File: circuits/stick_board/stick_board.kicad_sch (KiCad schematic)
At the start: 8 parts, among them U1 GULI, U2 GULI, U5 DRV5055A1xDBZxQ1, U6 DRV5055A1xDBZxQ1

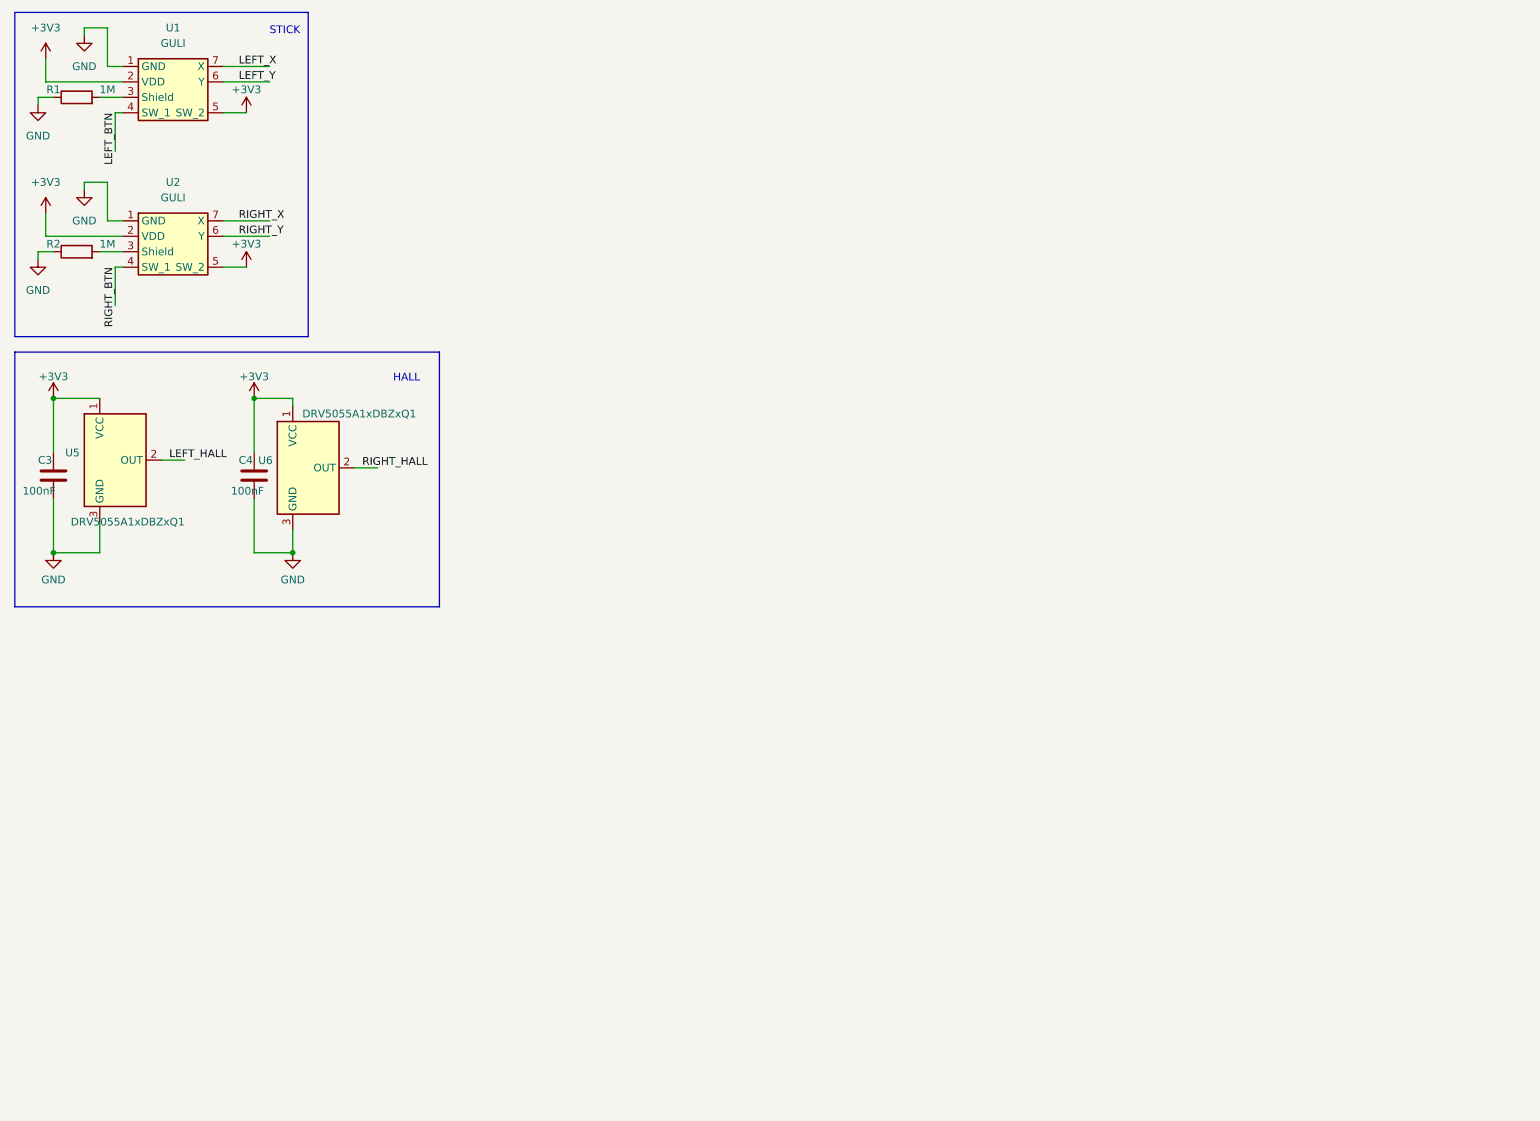
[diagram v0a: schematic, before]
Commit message: add mcu board
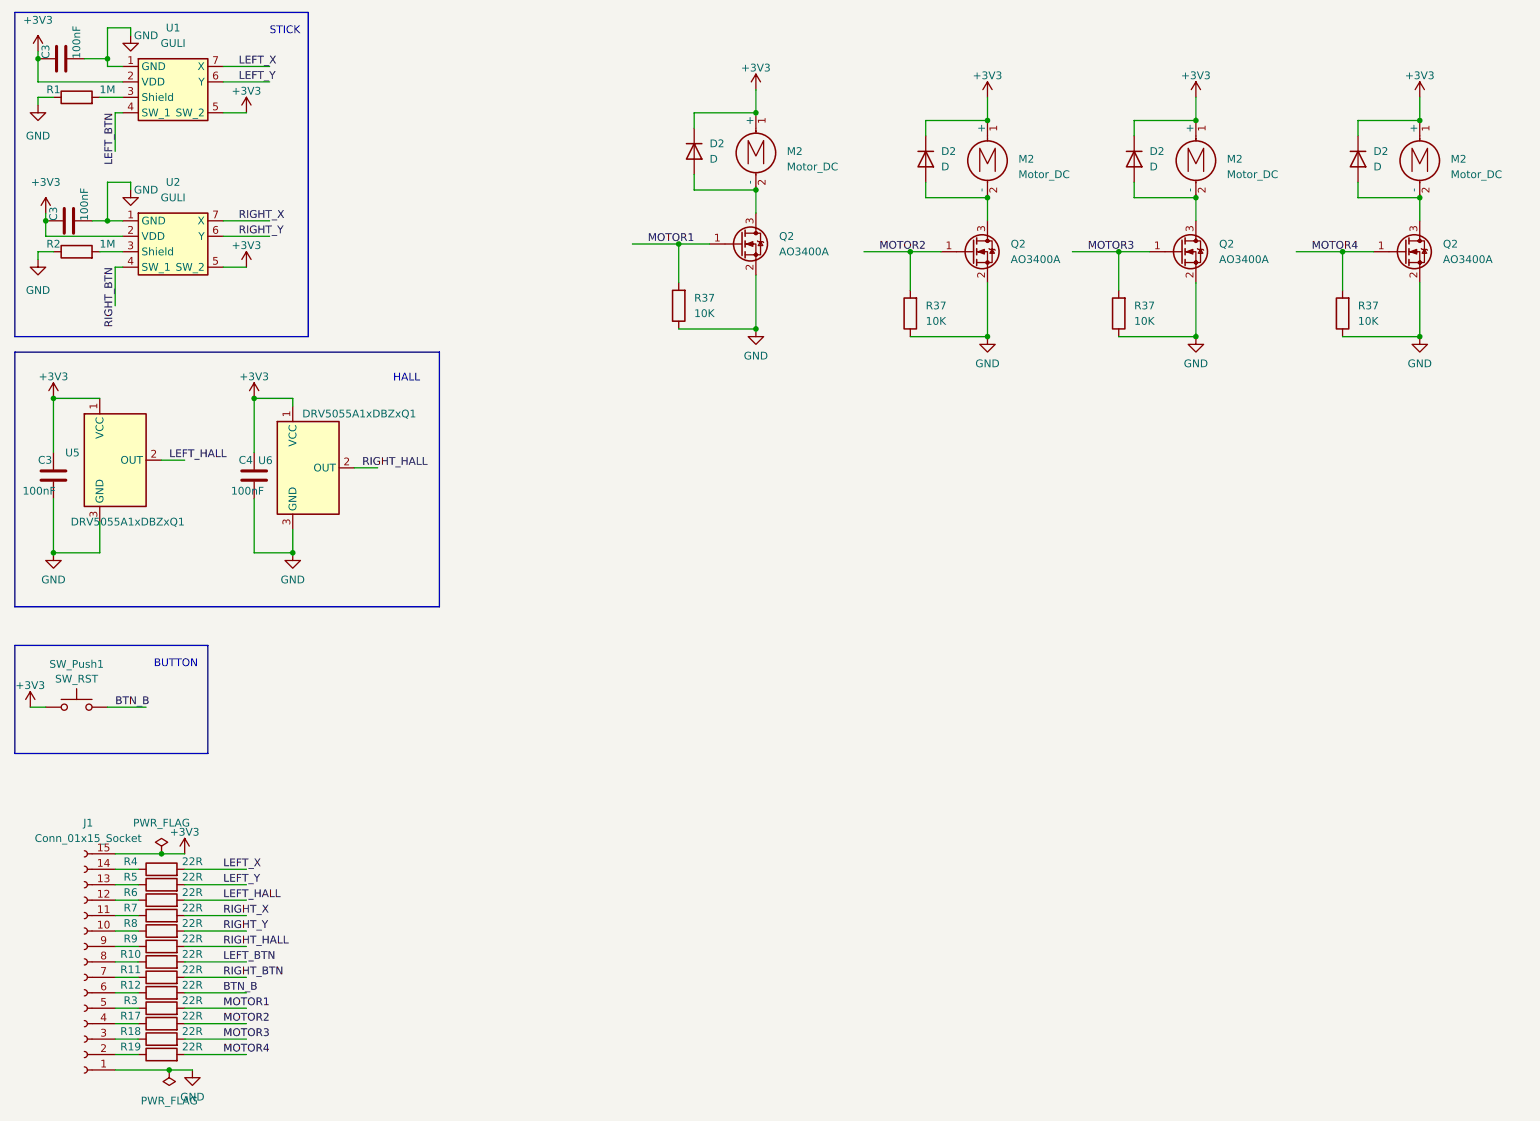
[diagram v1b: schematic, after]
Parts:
- added C3 (x2): 100nF, Resistor_SMD:R_0805_2012Metric_Pad1.20x1.40mm_HandSolder, symbol Device:C
- added D2 (x4): D, Diode_SMD:D_0805_2012Metric_Pad1.15x1.40mm_HandSolder, symbol Device:D
- added J1: Conn_01x15_Socket, symbol Connector:Conn_01x15_Socket
- added M2 (x4): Motor_DC, Resistor_SMD:R_1210_3225Metric_Pad1.30x2.65mm_HandSolder, symbol Motor:Motor_DC
- added Q2 (x4): AO3400A, Package_TO_SOT_SMD:SOT-23-3, symbol Transistor_FET:AO3400A
- added R10, R11, R12, R17, R18, R19, R3, R4, R5, R6, R7, R8, R9: 22R, symbol Device:R
- added R37 (x4): 10K, Resistor_SMD:R_0805_2012Metric_Pad1.20x1.40mm_HandSolder, symbol Device:R
- added SW_Push1: SW_RST, Button_Switch_THT:SW_PUSH_6mm_H4.3mm, symbol Switch:SW_Push
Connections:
- net +3V3: now also C3.1, C3.1, D2.1 (K), D2.1 (K), D2.1 (K), D2.1 (K), J1.15 (Pin_15), M2.1 (+), M2.1 (+), M2.1 (+), M2.1 (+), SW_Push1.1
- net GND: now also C3.2, C3.2, J1.1 (Pin_1), Q2.2 (S), Q2.2 (S), Q2.2 (S), Q2.2 (S), R37.1, R37.1, R37.1, R37.1
- net LEFT_BTN: now also R10.2
- net LEFT_HALL: now also R6.2
- net LEFT_X: now also R4.2
- net LEFT_Y: now also R5.2
- net RIGHT_BTN: now also R11.2
- net RIGHT_HALL: now also R9.2
- net RIGHT_X: now also R7.2
- net RIGHT_Y: now also R8.2
- new net: D2.2 (A), M2.2 (-), Q2.3 (D) (x4)
- new net: J1.2 (Pin_2), R19.1
- new net: J1.4 (Pin_4), R17.1
- new net: J1.13 (Pin_13), R5.1
- new net: J1.3 (Pin_3), R18.1
- new net: J1.11 (Pin_11), R7.1
- new net: J1.9 (Pin_9), R9.1
- new net: J1.8 (Pin_8), R10.1
- new net: J1.14 (Pin_14), R4.1
- new net: J1.10 (Pin_10), R8.1
- new net: J1.12 (Pin_12), R6.1
- new net: J1.5 (Pin_5), R3.1
- new net: J1.6 (Pin_6), R12.1
- new net: J1.7 (Pin_7), R11.1
- new net BTN_B: R12.2, SW_Push1.2
- new net MOTOR1: Q2.1 (G), R3.2, R37.2
- new net MOTOR2: Q2.1 (G), R17.2, R37.2
- new net MOTOR3: Q2.1 (G), R18.2, R37.2
- new net MOTOR4: Q2.1 (G), R19.2, R37.2
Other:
- note added: "BUTTON"

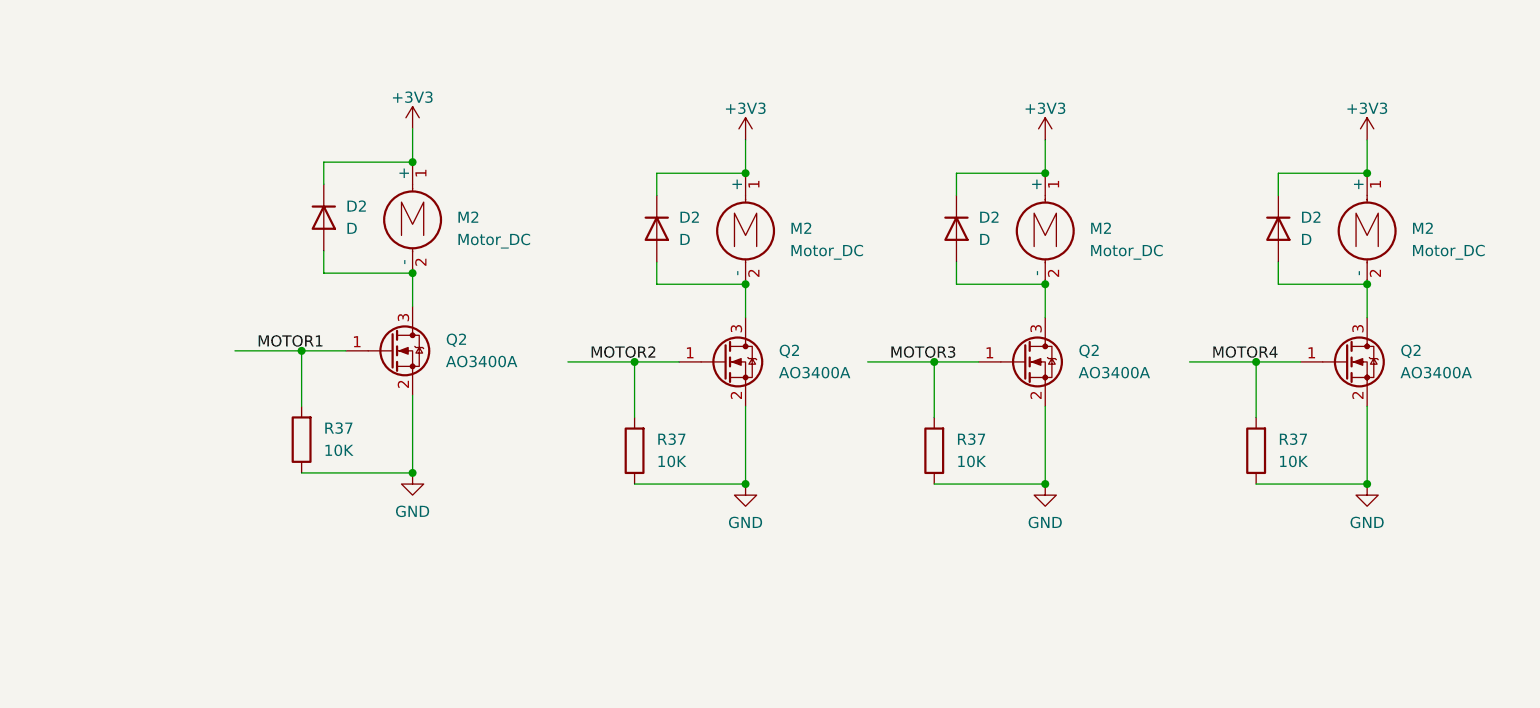
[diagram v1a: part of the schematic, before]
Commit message: pwm和led初步测试ok
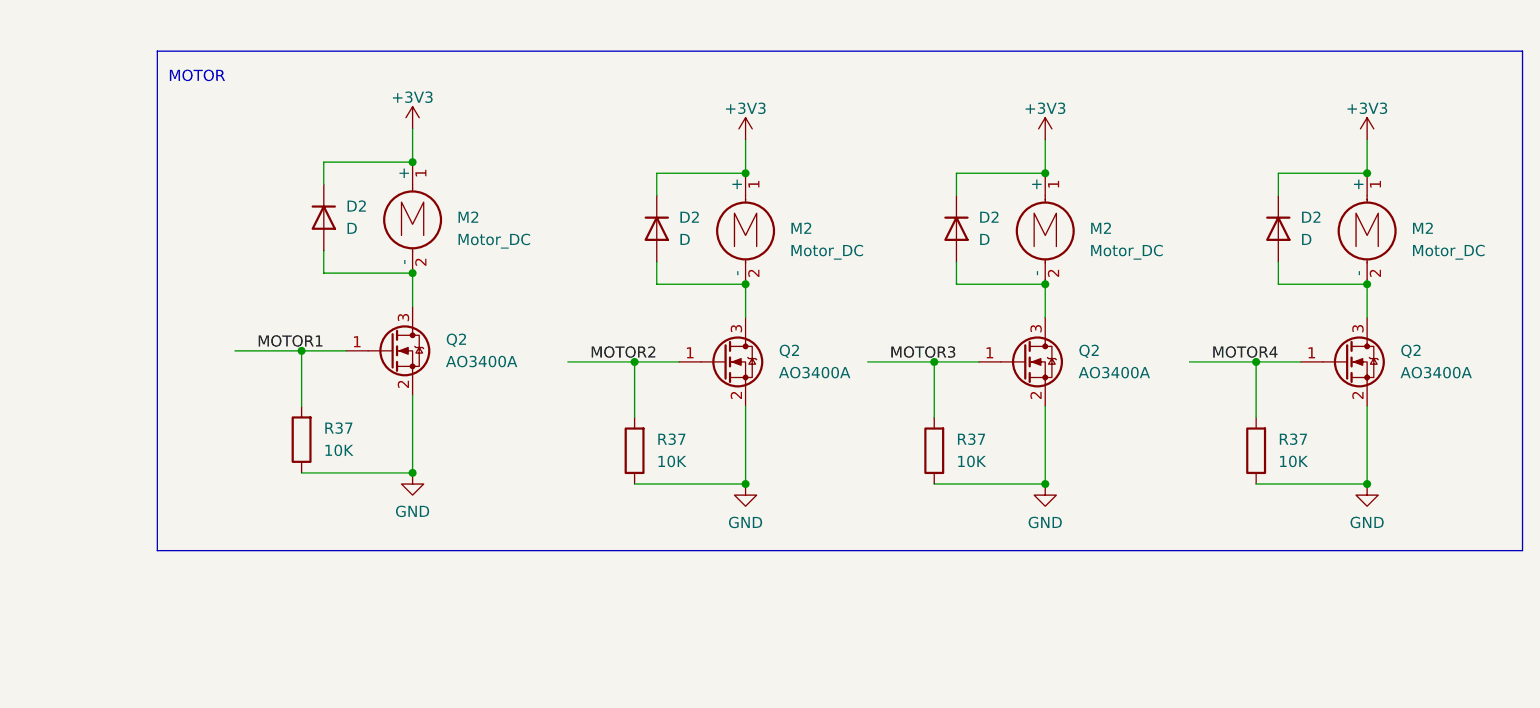
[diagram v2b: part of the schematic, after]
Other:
- note added: "MOTOR"
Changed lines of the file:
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@@
     (stroke (width 0) (type default))
+  )
+  (rectangle (start 106.68 17.78) (end 262.89 74.93)
+    (stroke (width 0) (type default))
+    (fill (type none))
   )
   (rectangle (start 13.97 118.11) (end 45.72 135.89)
@@
     (fill (type none))
   )
+  (text "MOTOR" (at 107.95 21.59 0)
+    (effects (font (size 1.27 1.27)) (justify left bottom))
+  )
   (text "STICK" (at 55.88 17.78 0)
